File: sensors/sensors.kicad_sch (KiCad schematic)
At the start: 9 parts, among them J1 GPIO, J2 JP_CAN, J3 JP_PWM, J4 JP_ADC

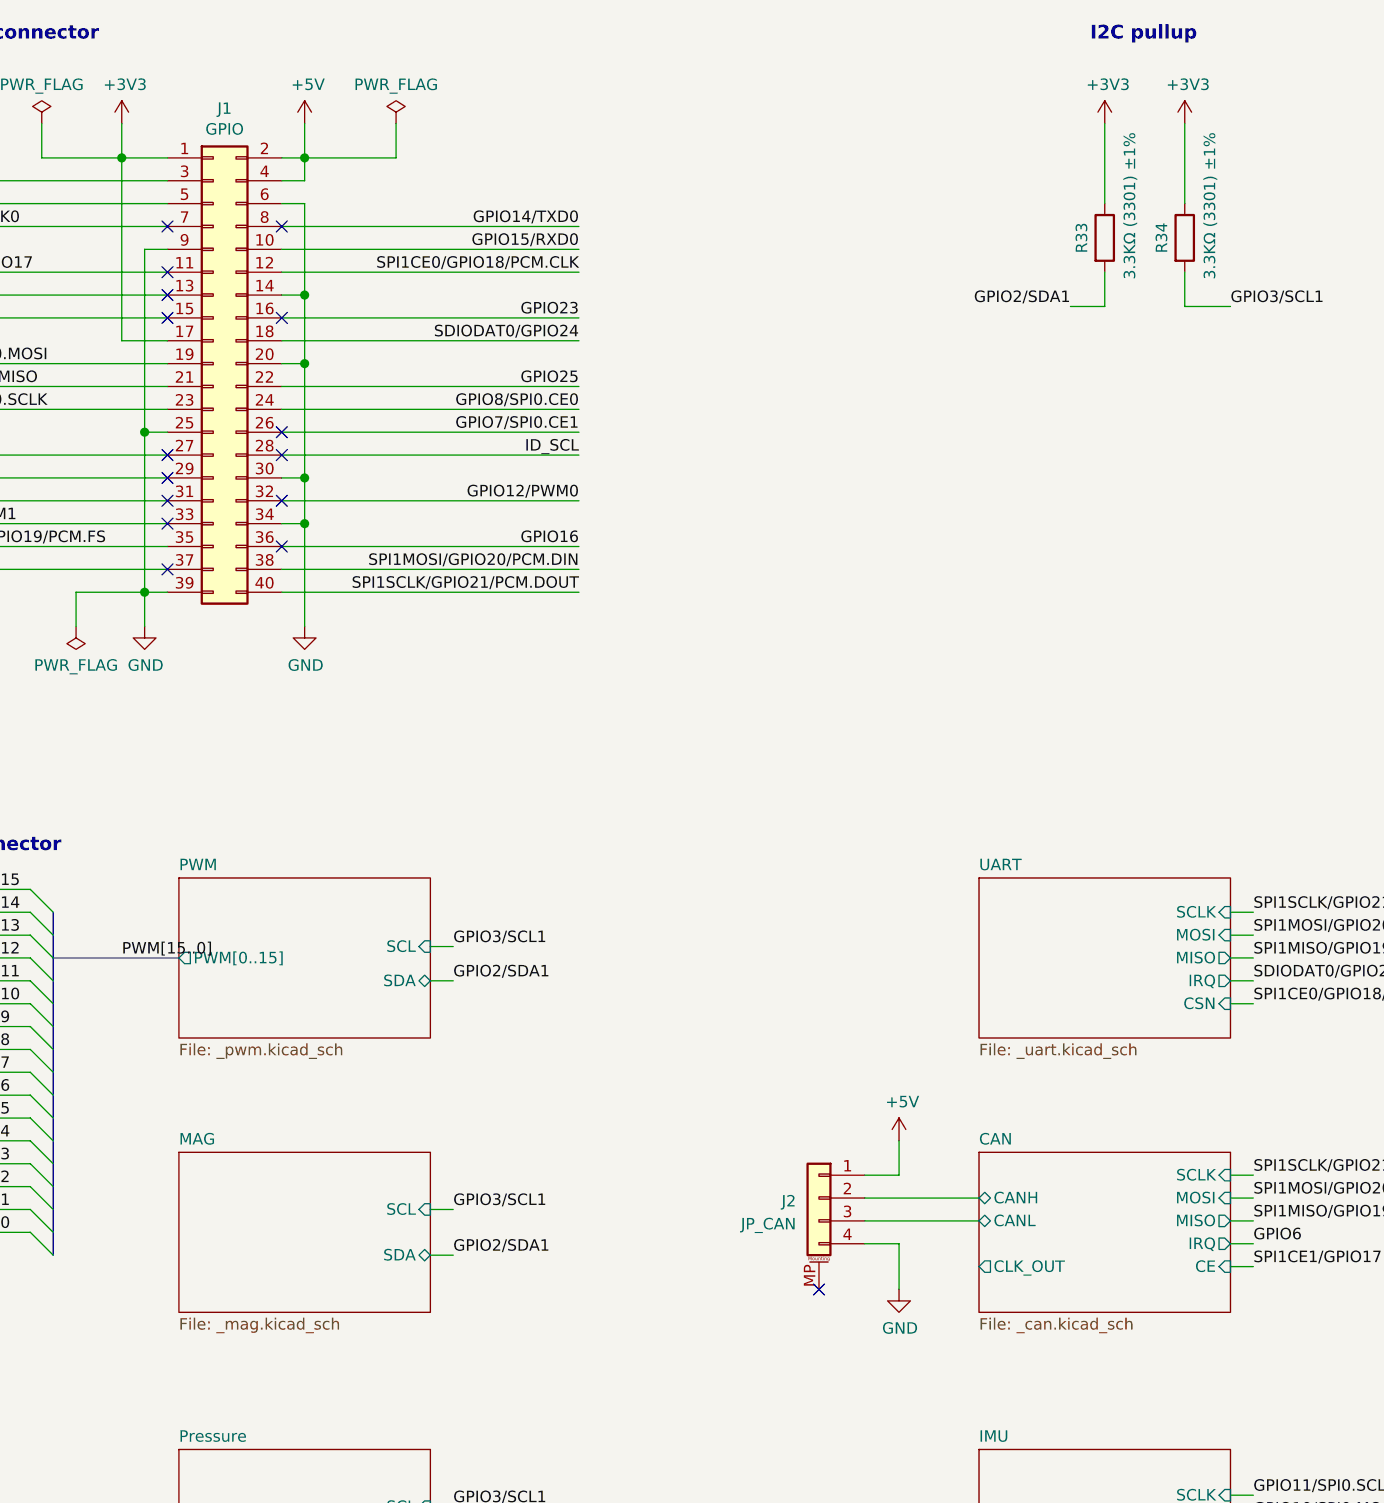
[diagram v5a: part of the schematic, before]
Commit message: use CLK out from CAN controller for UART (use 16 MHz instead of 14.7456MHz); minor changes
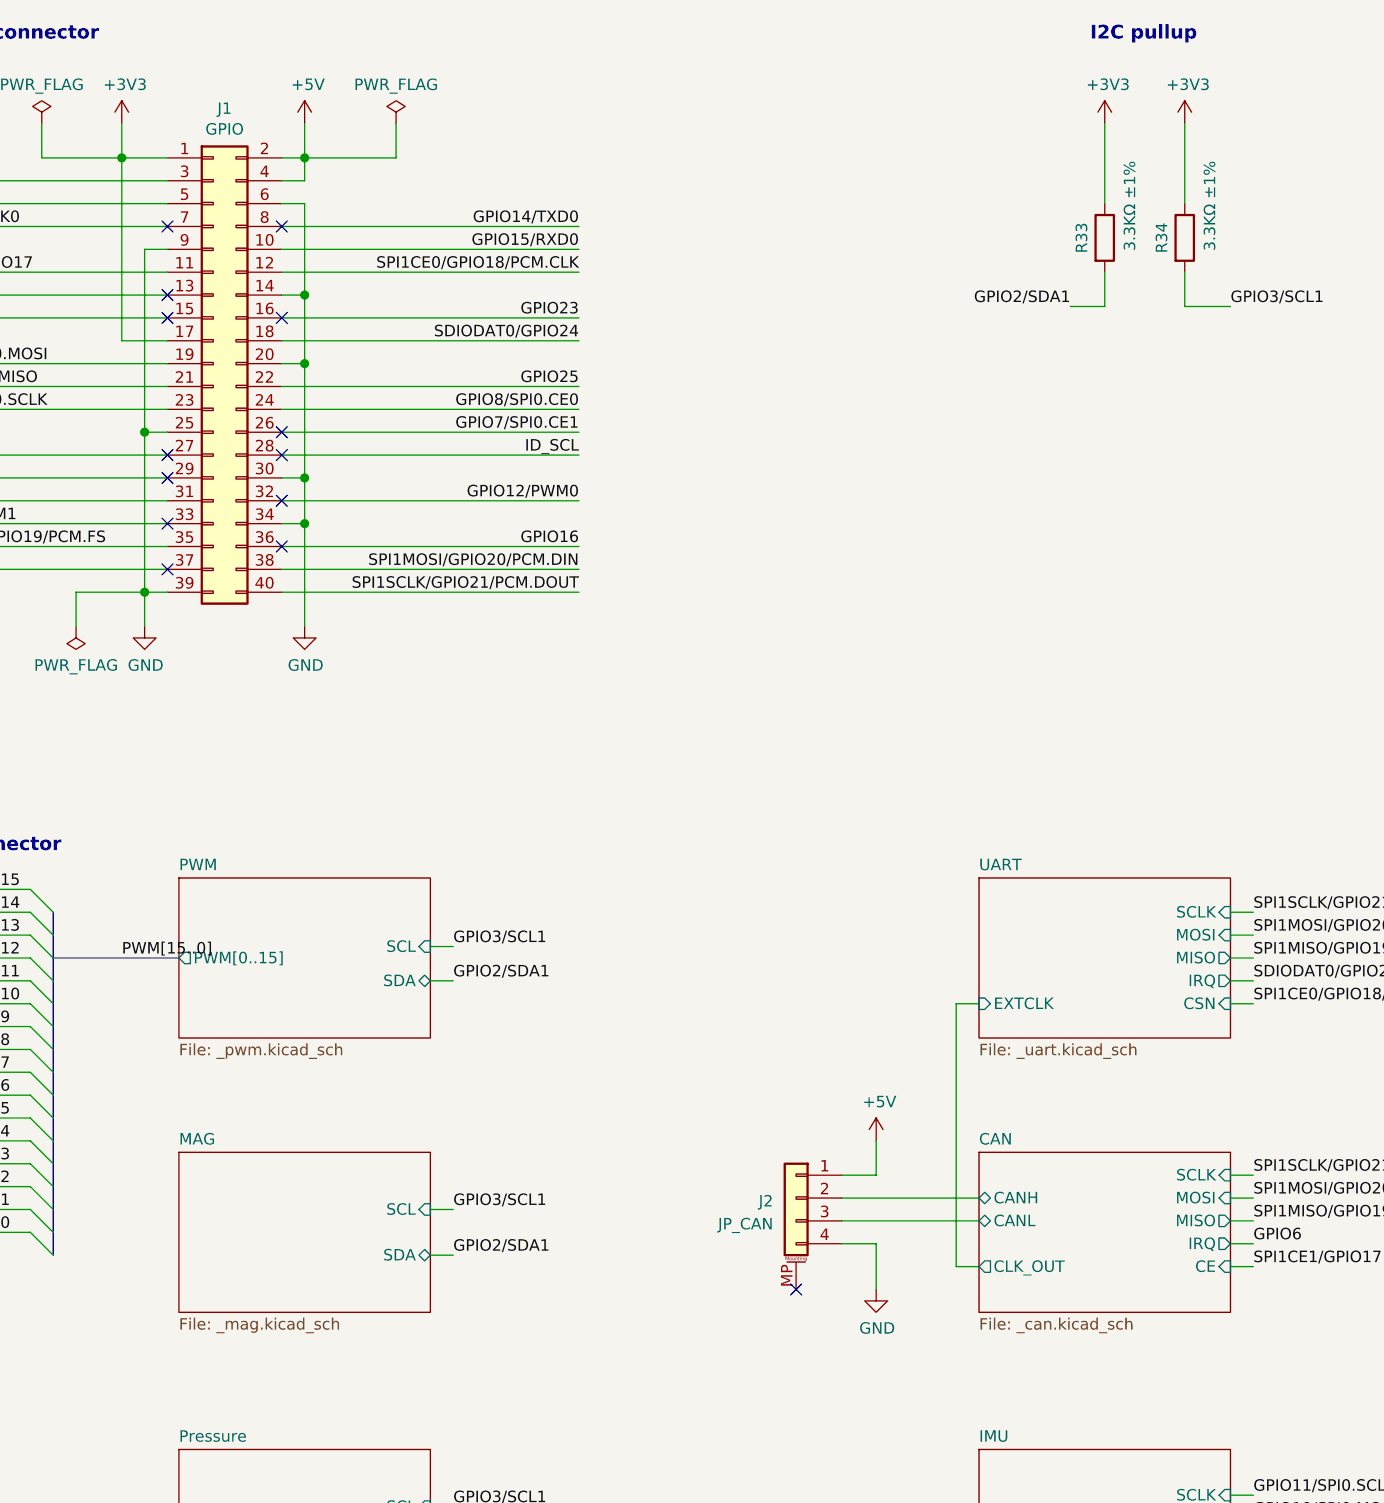
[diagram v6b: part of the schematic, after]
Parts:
- R33, R34: value 3.3KΩ (3301) ±1% -> 3.3KΩ ±1%
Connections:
- no-connect marks 16 -> 14
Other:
- sheet UART ports: added EXTCLK; removed none
- moved on the sheet: J2
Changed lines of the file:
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@@
 	)
 	(no_connect
-		(at 60.96 74.93)
-	)
-	(no_connect
 		(at 73.66 54.61)
 	)
@@
 	)
 	(no_connect
-		(at 60.96 49.53)
-	)
-	(no_connect
-		(at 133.35 162.56)
+		(at 130.81 162.56)
 	)
 	(no_connect
@@
 	(wire
 		(pts
+			(xy 148.59 160.02) (xy 151.13 160.02)
+		)
+		(stroke
+			(width 0)
+			(type default)
+		)
+	)
+	(wire
+		(pts
 			(xy 76.2 59.69) (xy 76.2 72.39)
 		)
@@
 	(wire
 		(pts
-			(xy 138.43 152.4) (xy 151.13 152.4)
+			(xy 135.89 152.4) (xy 151.13 152.4)
 		)
 		(stroke
@@
 	(wire
 		(pts
-			(xy 138.43 154.94) (xy 151.13 154.94)
+			(xy 135.89 154.94) (xy 151.13 154.94)
 		)
 		(stroke
@@
 	(wire
 		(pts
-			(xy 142.24 149.86) (xy 138.43 149.86)
+			(xy 139.7 149.86) (xy 135.89 149.86)
 		)
 		(stroke
@@
 	(wire
 		(pts
-			(xy 142.24 146.05) (xy 142.24 149.86)
+			(xy 139.7 146.05) (xy 139.7 149.86)
 		)
 		(stroke
@@
 	(wire
 		(pts
+			(xy 148.59 130.81) (xy 148.59 160.02)
+		)
+		(stroke
+			(width 0)
+			(type default)
+		)
+	)
+	(wire
+		(pts
 			(xy 86.36 33.02) (xy 86.36 36.83)
 		)
@@
 	(wire
 		(pts
-			(xy 138.43 157.48) (xy 142.24 157.48)
+			(xy 135.89 157.48) (xy 139.7 157.48)
 		)
 		(stroke
@@
 	(wire
 		(pts
-			(xy 142.24 157.48) (xy 142.24 162.56)
+			(xy 139.7 157.48) (xy 139.7 162.56)
 		)
 		(stroke
@@
 	(wire
 		(pts
+			(xy 148.59 130.81) (xy 151.13 130.81)
+		)
+		(stroke
+			(width 0)
+			(type default)
+		)
+	)
+	(wire
+		(pts
 			(xy 55.88 36.83) (xy 60.96 36.83)
 		)
@@
 			)
 		)
-		(property "Value" "3.3KΩ (3301) ±1%"
+		(property "Value" "3.3KΩ ±1%"
 			(at 176.784 42.164 90)
 			(show_name no)
@@
 	(symbol
 		(lib_id "power:GND")
-		(at 142.24 162.56 0)
+		(at 139.7 162.56 0)
 		(unit 1)
 		(body_style 1)
@@
 		(dnp no)
 		(property "Reference" "#PWR089"
-			(at 142.24 168.91 0)
+			(at 139.7 168.91 0)
 			(hide yes)
 			(show_name no)
@@
 		)
 		(property "Value" "GND"
-			(at 142.3543 166.8844 0)
+			(at 139.8143 166.8844 0)
 			(show_name no)
 			(do_not_autoplace no)
@@
 		)
 		(property "Footprint" ""
-			(at 142.24 162.56 0)
+			(at 139.7 162.56 0)
 			(show_name no)
 			(do_not_autoplace no)
@@
 		)
 		(property "Datasheet" ""
-			(at 142.24 162.56 0)
+			(at 139.7 162.56 0)
 			(show_name no)
 			(do_not_autoplace no)
@@
 		)
 		(property "Description" "Power symbol creates a global label with name \"GND\" , ground"
-			(at 142.24 162.56 0)
+			(at 139.7 162.56 0)
 			(hide yes)
 			(show_name no)
@@
 	(symbol
 		(lib_id "power:+5V")
-		(at 142.24 146.05 0)
+		(at 139.7 146.05 0)
 		(unit 1)
 		(body_style 1)
@@
 		(dnp no)
 		(property "Reference" "#PWR090"
-			(at 142.24 149.86 0)
+			(at 139.7 149.86 0)
 			(hide yes)
 			(show_name no)
@@
 		)
 		(property "Value" "+5V"
-			(at 142.6083 141.7256 0)
+			(at 140.0683 141.7256 0)
 			(show_name no)
 			(do_not_autoplace no)
@@
 		)
 		(property "Footprint" ""
-			(at 142.24 146.05 0)
+			(at 139.7 146.05 0)
 			(show_name no)
 			(do_not_autoplace no)
@@
 		)
 		(property "Datasheet" ""
-			(at 142.24 146.05 0)
+			(at 139.7 146.05 0)
 			(show_name no)
 			(do_not_autoplace no)
@@
 		)
 		(property "Description" "Power symbol creates a global label with name \"+5V\""
-			(at 142.24 146.05 0)
+			(at 139.7 146.05 0)
 			(hide yes)
 			(show_name no)
@@
 			)
 		)
-		(property "Value" "3.3KΩ (3301) ±1%"
+		(property "Value" "3.3KΩ ±1%"
 			(at 167.894 42.164 90)
 			(show_name no)
@@
 	(symbol
 		(lib_id "Connector_Generic_MountingPin:Conn_01x04_MountingPin")
-		(at 133.35 152.4 0)
+		(at 130.81 152.4 0)
 		(mirror y)
 		(unit 1)
@@
 		(dnp no)
 		(property "Reference" "J2"
-			(at 130.81 152.7555 0)
+			(at 128.27 152.7555 0)
 			(show_name no)
 			(do_not_autoplace no)
@@
 		)
 		(property "Value" "JP_CAN"
-			(at 130.81 155.2955 0)
+			(at 128.27 155.2955 0)
 			(show_name no)
 			(do_not_autoplace no)
@@
 		)
 		(property "Footprint" "Connector_JST:JST_GH_BM04B-GHS-TBT_1x04-1MP_P1.25mm_Vertical"
-			(at 133.35 152.4 0)
+			(at 130.81 152.4 0)
 			(hide yes)
 			(show_name no)
@@
 		)
 		(property "Datasheet" ""
-			(at 133.35 152.4 0)
+			(at 130.81 152.4 0)
 			(hide yes)
 			(show_name no)
@@
 		)
 		(property "Description" "Generic connectable mounting pin connector, single row, 01x04, script generated (kicad-library-utils/schlib/autogen/connector/)"
-			(at 133.35 152.4 0)
+			(at 130.81 152.4 0)
 			(hide yes)
 			(show_name no)
@@
 		)
 		(property "Part" ""
-			(at 133.35 152.4 0)
+			(at 130.81 152.4 0)
 			(hide yes)
 			(show_name no)
@@
 			)
 		)
+		(pin "EXTCLK" input
+			(at 151.13 130.81 180)
+			(effects
+				(font
+					(size 1.27 1.27)
+				)
+				(justify left)
+			)
+		)

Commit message: minor changes
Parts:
- J1: Part (none) -> F185-1220A0ASYE3
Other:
- moved on the sheet: J3
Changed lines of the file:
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@@
 	(text "PWM Connector"
 		(exclude_from_sim no)
-		(at 39.8165 113.284 0)
+		(at 30.9265 113.284 0)
 		(effects
 			(font
@@
 	)
 	(bus_entry
-		(at 45.72 135.89)
+		(at 36.83 135.89)
 		(size 2.54 2.54)
 		(stroke
@@
 	)
 	(bus_entry
-		(at 45.72 138.43)
+		(at 36.83 138.43)
 		(size 2.54 2.54)
 		(stroke
@@
 	)
 	(bus_entry
-		(at 45.72 125.73)
+		(at 36.83 125.73)
 		(size 2.54 2.54)
 		(stroke
@@
 	)
 	(bus_entry
-		(at 45.72 153.67)
+		(at 36.83 153.67)
 		(size 2.54 2.54)
 		(stroke
@@
 	)
 	(bus_entry
-		(at 45.72 123.19)
+		(at 36.83 123.19)
 		(size 2.54 2.54)
 		(stroke
@@
 	)
 	(bus_entry
-		(at 45.72 151.13)
+		(at 36.83 151.13)
 		(size 2.54 2.54)
 		(stroke
@@
 	)
 	(bus_entry
-		(at 45.72 120.65)
+		(at 36.83 120.65)
 		(size 2.54 2.54)
 		(stroke
@@
 	)
 	(bus_entry
-		(at 45.72 133.35)
+		(at 36.83 133.35)
 		(size 2.54 2.54)
 		(stroke
@@
 	)
 	(bus_entry
-		(at 45.72 148.59)
+		(at 36.83 148.59)
 		(size 2.54 2.54)
 		(stroke
@@
 	)
 	(bus_entry
-		(at 45.72 146.05)
+		(at 36.83 146.05)
 		(size 2.54 2.54)
 		(stroke
@@
 	)
 	(bus_entry
-		(at 45.72 156.21)
+		(at 36.83 156.21)
 		(size 2.54 2.54)
 		(stroke
@@
 	)
 	(bus_entry
-		(at 45.72 118.11)
+		(at 36.83 118.11)
 		(size 2.54 2.54)
 		(stroke
@@
 	)
 	(bus_entry
-		(at 45.72 128.27)
+		(at 36.83 128.27)
 		(size 2.54 2.54)
 		(stroke
@@
 	)
 	(bus_entry
-		(at 45.72 140.97)
+		(at 36.83 140.97)
 		(size 2.54 2.54)
 		(stroke
@@
 	)
 	(bus_entry
-		(at 45.72 143.51)
+		(at 36.83 143.51)
 		(size 2.54 2.54)
 		(stroke
@@
 	)
 	(bus_entry
-		(at 45.72 130.81)
+		(at 36.83 130.81)
 		(size 2.54 2.54)
 		(stroke
@@
 	(wire
 		(pts
-			(xy 38.1 135.89) (xy 45.72 135.89)
+			(xy 29.21 135.89) (xy 36.83 135.89)
 		)
 		(stroke
@@
 	(wire
 		(pts
-			(xy 38.1 146.05) (xy 45.72 146.05)
+			(xy 29.21 146.05) (xy 36.83 146.05)
 		)
 		(stroke
@@
 	(wire
 		(pts
-			(xy 38.1 133.35) (xy 45.72 133.35)
+			(xy 29.21 133.35) (xy 36.83 133.35)
 		)
 		(stroke
@@
 	(wire
 		(pts
-			(xy 38.1 120.65) (xy 45.72 120.65)
+			(xy 29.21 120.65) (xy 36.83 120.65)
 		)
 		(stroke
@@
 	(wire
 		(pts
+			(xy 261.62 125.73) (xy 266.7 125.73)
+		)
+		(stroke
+			(width 0)
+			(type default)
+		)
+	)
+	(wire
+		(pts
 			(xy 76.2 59.69) (xy 76.2 72.39)
 		)
@@
 	(wire
 		(pts
-			(xy 38.1 118.11) (xy 45.72 118.11)
+			(xy 29.21 118.11) (xy 36.83 118.11)
 		)
 		(stroke
@@
 	(wire
 		(pts
-			(xy 38.1 148.59) (xy 45.72 148.59)
+			(xy 29.21 148.59) (xy 36.83 148.59)
 		)
 		(stroke
@@
 	(wire
 		(pts
-			(xy 38.1 138.43) (xy 45.72 138.43)
+			(xy 29.21 138.43) (xy 36.83 138.43)
 		)
 		(stroke
@@
 	(wire
 		(pts
-			(xy 261.62 127) (xy 266.7 127)
-		)
-		(stroke
-			(width 0)
-			(type default)
-		)
-	)
-	(wire
-		(pts
 			(xy 58.42 67.31) (xy 60.96 67.31)
 		)
@@
 	(wire
 		(pts
-			(xy 38.1 123.19) (xy 45.72 123.19)
+			(xy 29.21 123.19) (xy 36.83 123.19)
 		)
 		(stroke
@@
 	(wire
 		(pts
-			(xy 38.1 143.51) (xy 45.72 143.51)
+			(xy 29.21 143.51) (xy 36.83 143.51)
 		)
 		(stroke
@@
 	(wire
 		(pts
-			(xy 38.1 130.81) (xy 45.72 130.81)
+			(xy 29.21 130.81) (xy 36.83 130.81)
 		)
 		(stroke
@@
 	(bus
 		(pts
-			(xy 48.26 125.73) (xy 48.26 120.65)
+			(xy 39.37 125.73) (xy 39.37 120.65)
 		)
 		(stroke
@@
 	(bus
 		(pts
-			(xy 48.26 125.73) (xy 48.26 158.75)
+			(xy 39.37 125.73) (xy 39.37 158.75)
 		)
 		(stroke
@@
 	(wire
 		(pts
-			(xy 38.1 140.97) (xy 45.72 140.97)
+			(xy 29.21 140.97) (xy 36.83 140.97)
 		)
 		(stroke
@@
 	(wire
 		(pts
-			(xy 38.1 125.73) (xy 45.72 125.73)
+			(xy 29.21 125.73) (xy 36.83 125.73)
 		)
 		(stroke
@@
 	(wire
 		(pts
-			(xy 38.1 151.13) (xy 45.72 151.13)
+			(xy 29.21 151.13) (xy 36.83 151.13)
 		)
 		(stroke
@@
 	(wire
 		(pts
-			(xy 38.1 153.67) (xy 45.72 153.67)
+			(xy 29.21 153.67) (xy 36.83 153.67)
 		)
 		(stroke
@@
 	(wire
 		(pts
-			(xy 38.1 128.27) (xy 45.72 128.27)
+			(xy 29.21 128.27) (xy 36.83 128.27)
 		)
 		(stroke
@@
 	(wire
 		(pts
-			(xy 38.1 156.21) (xy 45.72 156.21)
+			(xy 29.21 156.21) (xy 36.83 156.21)
 		)
 		(stroke
@@
 	(bus
 		(pts
-			(xy 48.26 125.73) (xy 62.23 125.73)
+			(xy 39.37 125.73) (xy 62.23 125.73)
 		)
 		(stroke
@@
 	)
 	(label "PWM0"
-		(at 38.1 156.21 0)
+		(at 29.21 156.21 0)
 		(effects
 			(font
@@
 	)
 	(label "PWM13"
-		(at 38.1 123.19 0)
+		(at 29.21 123.19 0)
 		(effects
 			(font
@@
 	)
 	(label "PWM5"
-		(at 38.1 143.51 0)
+		(at 29.21 143.51 0)
 		(effects
 			(font
@@
 	)
 	(label "PWM7"
-		(at 38.1 138.43 0)
+		(at 29.21 138.43 0)
 		(effects
 			(font
@@
 	)
 	(label "PWM9"
-		(at 38.1 133.35 0)
+		(at 29.21 133.35 0)
 		(effects
 			(font
@@
 	)
 	(label "PWM4"
-		(at 38.1 146.05 0)
+		(at 29.21 146.05 0)
 		(effects
 			(font
@@
 	)
 	(label "PWM8"
-		(at 38.1 135.89 0)
+		(at 29.21 135.89 0)
 		(effects
 			(font
@@
 	)
 	(label "PWM6"
-		(at 38.1 140.97 0)
+		(at 29.21 140.97 0)
 		(effects
 			(font
@@
 	)
 	(label "PWM2"
-		(at 38.1 151.13 0)
+		(at 29.21 151.13 0)
 		(effects
 			(font
@@
 	)
 	(label "PWM11"
-		(at 38.1 128.27 0)
+		(at 29.21 128.27 0)
 		(effects
 			(font
@@
 	)
 	(label "RCIN"
-		(at 261.62 127 180)
+		(at 261.62 125.73 180)
 		(effects
 			(font
@@
 	)
 	(label "PWM12"
-		(at 38.1 125.73 0)
+		(at 29.21 125.73 0)
 		(effects
 			(font
@@
 	)
 	(label "PWM10"
-		(at 38.1 130.81 0)
+		(at 29.21 130.81 0)
 		(effects
 			(font
@@
 	)
 	(label "PWM1"
-		(at 38.1 153.67 0)
+		(at 29.21 153.67 0)
 		(effects
 			(font
@@
 	)
 	(label "PWM3"
-		(at 38.1 148.59 0)
+		(at 29.21 148.59 0)
 		(effects
 			(font
@@
 	)
 	(label "PWM15"
-		(at 38.1 118.11 0)
+		(at 29.21 118.11 0)
 		(effects
 			(font
@@
 	)
 	(label "PWM14"
-		(at 38.1 120.65 0)
+		(at 29.21 120.65 0)
 		(effects
 			(font
@@
 	)
 	(label "PWM[15..0]"
-		(at 55.88 125.73 0)
+		(at 46.99 125.73 0)
 		(effects
 			(font
@@
 			)
 		)
+		(property "Part" "F185-1220A0ASYE3"
+			(at 66.04 59.69 0)
+			(hide yes)
+			(show_name no)
+			(do_not_autoplace no)
+			(effects
+				(font
+					(size 1.27 1.27)
+				)
+			)
+		)
 		(pin "1"
 		)
@@
 	(symbol
 		(lib_id "Connector_Generic:Conn_01x16")
-		(at 33.02 138.43 180)
+		(at 24.13 138.43 180)
 		(unit 1)
 		(body_style 1)
@@
 		(dnp no)
 		(property "Reference" "J3"
-			(at 33.02 159.766 0)
+			(at 24.13 159.766 0)
 			(show_name no)
 			(do_not_autoplace no)
@@
 		)
 		(property "Value" "JP_PWM"
-			(at 33.02 162.306 0)
+			(at 24.13 162.306 0)
 			(show_name no)
 			(do_not_autoplace no)
@@
 		)
 		(property "Footprint" "Connector_PinHeader_2.54mm:PinHeader_1x16_P2.54mm_Vertical"
-			(at 33.02 138.43 0)
+			(at 24.13 138.43 0)
 			(hide yes)
 			(show_name no)
@@
 		)
 		(property "Datasheet" ""
-			(at 33.02 138.43 0)
+			(at 24.13 138.43 0)
 			(hide yes)
 			(show_name no)
@@
 		)
 		(property "Description" "Generic connector, single row, 01x16, script generated (kicad-library-utils/schlib/autogen/connector/)"
-			(at 33.02 138.43 0)
+			(at 24.13 138.43 0)
 			(hide yes)
 			(show_name no)
@@
 		)
 		(pin "RC" input
-			(at 266.7 127 180)
+			(at 266.7 125.73 180)
 			(effects
 				(font
